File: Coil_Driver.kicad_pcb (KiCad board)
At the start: 8 copper layers, 122.5 x 76 mm, 158 parts, among them J1 47346-0001, J3 NPPC122KFMS-RC, U1 SG-210STF 12.0000ML3, U10 ADP7142ARDZ-R7, U11 BUK9D23-40E, U12 BUK9D23-40E, U13 ADuM4120-1A, U14 ADuM4120-1A, U15 LT8253AJUFDM#PBF, U16 PSMNR55-40SSH, U17 PSMNR55-40SSH, U18 PSMNR55-40SSH, U19 PSMNR55-40SSH, U2 ICE40UP5K-SG48ITR, U20 BUK9D23-40E, U21 BUK9D23-40E, U22 PSMNR55-40SSH, U23 PSMNR55-40SSH, U24 PSMNR55-40SSH, U25 PSMNR55-40SSH, U26 LT3748, U27 BUK9D23-40E, U28 ADuM4120-1A, U29 ADuM4120-1A, U3 W25Q32JVSS, U4 SN74AUP2G125DCUR, U5 AP2127K-3.3, U6 LT1117CST#TRPBF, U7 AP2127K-1.2, U8 93LC56BT-I/OT, U9 FT232H

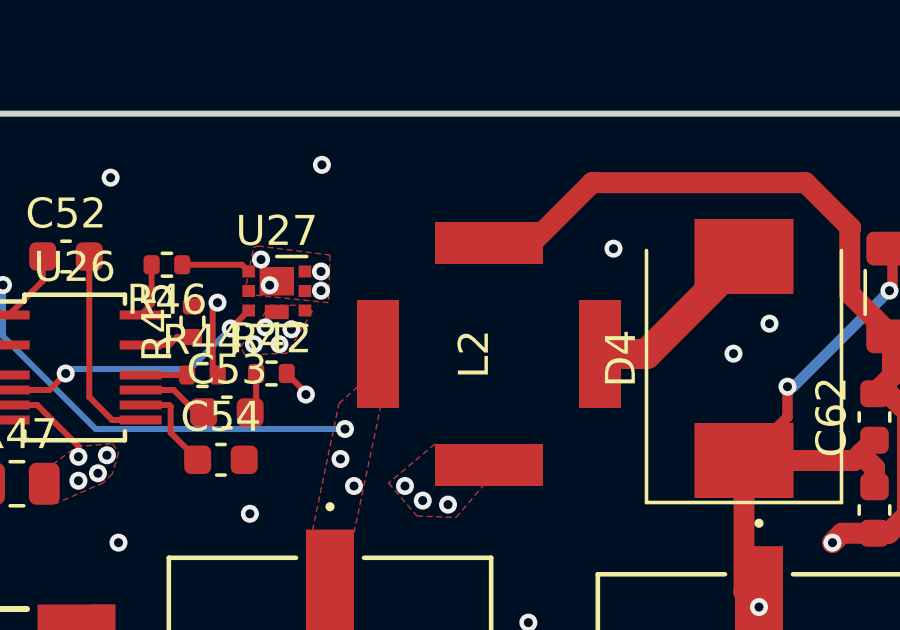
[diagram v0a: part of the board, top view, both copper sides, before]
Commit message: Rotated L2 90° clockwise
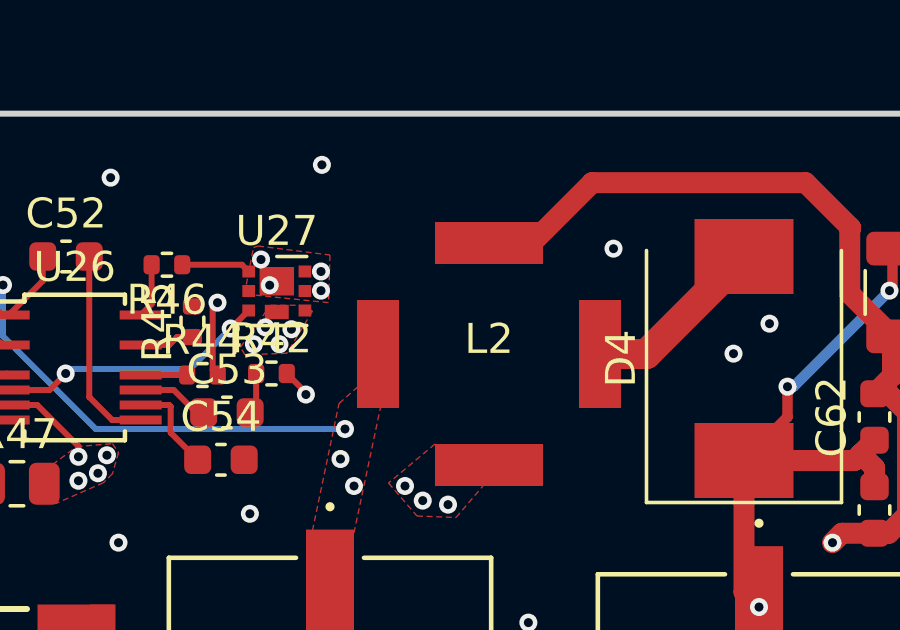
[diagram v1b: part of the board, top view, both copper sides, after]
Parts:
- turned L2 to 0 degrees
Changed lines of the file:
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@@
 	(footprint "New_Library:WE-TDC-8018"
 		(layer "F.Cu")
-		(at 85.45 32.01125 90)
+		(at 85.45 32.01125)
 		(property "Reference" "L2"
-			(at 0 -0.5 90)
+			(at 0 -0.5 0)
 			(unlocked yes)
 			(layer "F.SilkS")
@@
 		)
 		(property "Value" "74489430010"
-			(at 0 1 90)
+			(at 0 1 0)
 			(unlocked yes)
 			(layer "F.Fab")
@@
 		)
 		(property "Footprint" "New_Library:WE-TDC-8018"
-			(at 0 0 90)
+			(at 0 0 0)
 			(unlocked yes)
 			(layer "F.Fab")
@@
 		)
 		(property "Datasheet" "https://www.we-online.com/components/products/datasheet/74489430010.pdf"
-			(at 0 0 90)
+			(at 0 0 0)
 			(unlocked yes)
 			(layer "F.Fab")
@@
 		)
 		(property "Description" "1µ, 2.85a"
-			(at 0 0 90)
+			(at 0 0 0)
 			(unlocked yes)
 			(layer "F.Fab")
@@
 		)
 		(property "Sim.Device" "L"
-			(at 0 0 90)
+			(at 0 0 0)
 			(unlocked yes)
 			(layer "F.Fab")
@@
 		)
 		(property "Sim.Params" "L=74489430010"
-			(at 0 0 90)
+			(at 0 0 0)
 			(unlocked yes)
 			(layer "F.Fab")
@@
 		)
 		(fp_line
+			(start -4.6 -2)
+			(end -2 -4.6)
+			(stroke
+				(width 0.1)
+				(type default)
+			)
+			(layer "F.CrtYd")
+		)
+		(fp_line
+			(start -4.6 2)
+			(end -4.6 -2)
+			(stroke
+				(width 0.1)
+				(type default)
+			)
+			(layer "F.CrtYd")
+		)
+		(fp_line
+			(start -2 -4.6)
+			(end 2 -4.6)
+			(stroke
+				(width 0.1)
+				(type default)
+			)
+			(layer "F.CrtYd")
+		)
+		(fp_line
+			(start -2 4.6)
+			(end -4.6 2)
+			(stroke
+				(width 0.1)
+				(type default)
+			)
+			(layer "F.CrtYd")
+		)
+		(fp_line
 			(start 2 -4.6)
 			(end 4.6 -2)
@@
 		)
 		(fp_line
-			(start -2 -4.6)
-			(end 2 -4.6)
+			(start 2 4.6)
+			(end -2 4.6)
 			(stroke
 				(width 0.1)
@@
 		)
 		(fp_line
-			(start -4.6 -2)
-			(end -2 -4.6)
-			(stroke
-				(width 0.1)
-				(type default)
-			)
-			(layer "F.CrtYd")
-		)
-		(fp_line
 			(start 4.6 2)
 			(end 2 4.6)
@@
 			(layer "F.CrtYd")
 		)
-		(fp_line
-			(start -4.6 2)
-			(end -4.6 -2)
-			(stroke
-				(width 0.1)
-				(type default)
-			)
-			(layer "F.CrtYd")
-		)
-		(fp_line
-			(start 2 4.6)
-			(end -2 4.6)
-			(stroke
-				(width 0.1)
-				(type default)
-			)
-			(layer "F.CrtYd")
-		)
-		(fp_line
-			(start -2 4.6)
-			(end -4.6 2)
-			(stroke
-				(width 0.1)
-				(type default)
-			)
-			(layer "F.CrtYd")
-		)
 		(fp_text user "${REFERENCE}"
-			(at 0 2.5 90)
+			(at 0 2.5 0)
 			(unlocked yes)
 			(layer "F.Fab")
@@
 		)
 		(pad "1" smd rect
-			(at 0 -3.7 270)
+			(at 0 -3.7 180)
 			(size 3.6 1.4)
 			(layers "F.Cu" "F.Paste" "F.Mask")
@@
 		)
 		(pad "2" smd rect
-			(at -3.7 0 180)
+			(at -3.7 0 90)
 			(size 3.6 1.4)
 			(layers "F.Cu" "F.Paste" "F.Mask")
@@
 		)
 		(pad "3" smd rect
-			(at 0 3.7 270)
+			(at 0 3.7 180)
 			(size 3.6 1.4)
 			(layers "F.Cu" "F.Paste" "F.Mask")
@@
 		)
 		(pad "4" smd rect
-			(at 3.7 0)
+			(at 3.7 0 270)
 			(size 3.6 1.4)
 			(layers "F.Cu" "F.Paste" "F.Mask")
@@
 			(polygon
 				(pts
-					(xy 82.35 30.21125) (xy 83.65 28.91125) (xy 87.25 28.91125) (xy 88.55 30.21125) (xy 88.55 33.81125)
-					(xy 87.25 35.11125) (xy 83.65 35.11125) (xy 82.35 33.81125)
-				)
-			)
+					(xy 87.25 28.91125) (xy 88.55 30.21125) (xy 88.55 33.81125) (xy 87.25 35.11125) (xy 83.65 35.11125)
+					(xy 82.35 33.81125) (xy 82.35 30.21125) (xy 83.65 28.91125)
+				)
+			)

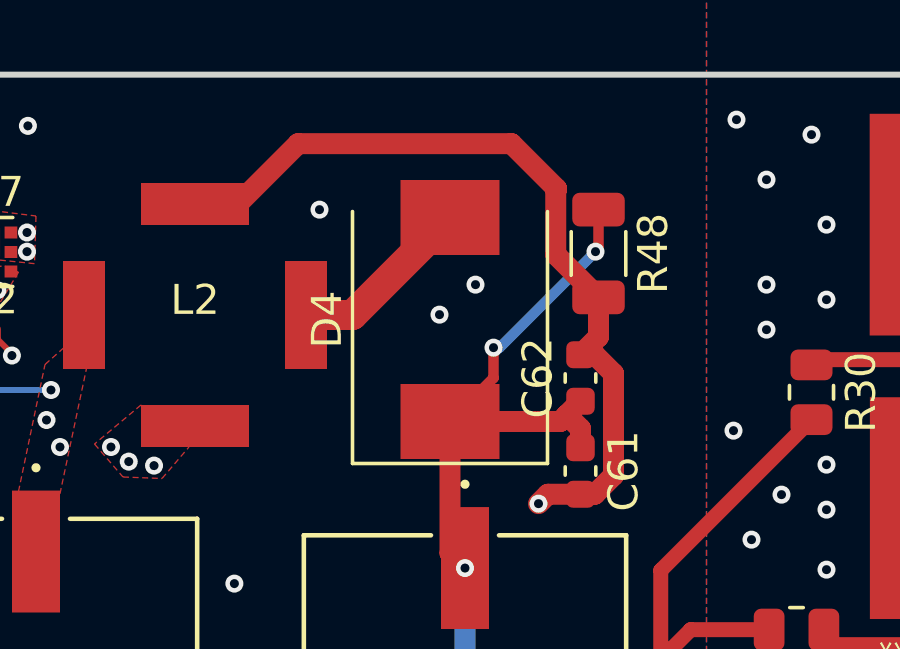
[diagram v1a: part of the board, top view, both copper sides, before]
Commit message: Fixed L2 symbol and PCB orientation
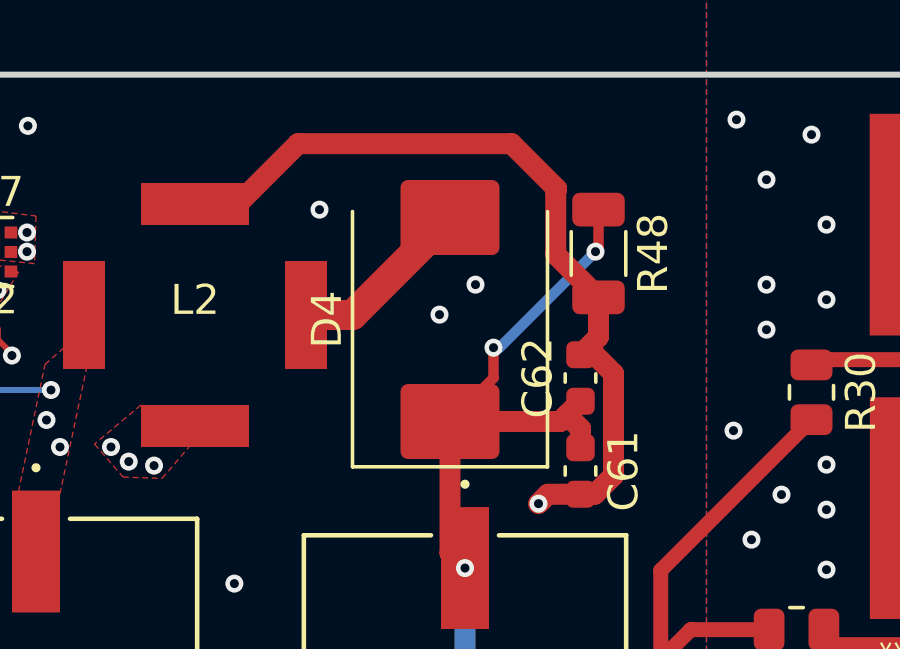
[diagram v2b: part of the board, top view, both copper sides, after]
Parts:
- R28, R47: value ESR10EZPF5R10 -> CRF0805-FZ-R005ELF
- R35: value 98.8k -> 95.3k
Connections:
- L2 pad 1: 10.5V -> GND2
- L2 pad 2: /toInductor -> 10.5V
- L2 pad 3: Net-(D4-A) -> /toInductor
- L2 pad 4: GND2 -> Net-(D4-A)
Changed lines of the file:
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@@
 			(size 3.6 1.4)
 			(layers "F.Cu" "F.Paste" "F.Mask")
-			(net 7 "10.5V")
-			(pinfunction "A")
+			(net 23 "GND2")
+			(pinfunction "1")
 			(pintype "passive")
 			(thermal_bridge_angle 45)
@@
 			(size 3.6 1.4)
 			(layers "F.Cu" "F.Paste" "F.Mask")
-			(net 134 "/toInductor")
-			(pinfunction "B")
+			(net 7 "10.5V")
+			(pinfunction "2")
 			(pintype "passive")
 			(thermal_bridge_angle 45)
@@
 			(size 3.6 1.4)
 			(layers "F.Cu" "F.Paste" "F.Mask")
-			(net 38 "Net-(D4-A)")
-			(pinfunction "B")
+			(net 134 "/toInductor")
+			(pinfunction "3")
 			(pintype "passive")
 			(thermal_bridge_angle 45)
@@
 			(size 3.6 1.4)
 			(layers "F.Cu" "F.Paste" "F.Mask")
-			(net 23 "GND2")
-			(pinfunction "A")
+			(net 38 "Net-(D4-A)")
+			(pinfunction "4")
 			(pintype "passive")
 			(thermal_bridge_angle 45)
@@
 			)
 		)
-		(model "/home/yeuph/Downloads/74489430010 (1)/Download_STP_WE-TDC-8018_rev1.stp"
-			(offset
-				(xyz 0 0 0)
-			)
-			(scale
-				(xyz 1 1 1)
-			)
-			(rotate
-				(xyz 0 0 0)
-			)
-		)
 	)
 	(footprint "Oscillator:Oscillator_SMD_SeikoEpson_SG210-4Pin_2.5x2.0mm"
@@
 			)
 		)
-		(property "Value" "98.8k"
+		(property "Value" "95.3k"
 			(at 0 1.17 0)
 			(layer "F.Fab")
@@
 			)
 		)
-		(property "Sim.Params" "R=98.8k"
+		(property "Sim.Params" "R=95.3k"
 			(at 0 0 180)
 			(unlocked yes)
@@
 		(attr smd)
 		(fp_line
-			(start -4.8 -3.25)
+			(start -4.91 -3.25)
 			(end 3.6 -3.25)
 			(stroke
@@
 		)
 		(fp_line
-			(start -4.8 3.25)
-			(end -4.8 -3.25)
+			(start -4.91 3.25)
+			(end -4.91 -3.25)
 			(stroke
 				(width 0.12)
@@
 		)
 		(fp_line
-			(start -4.8 3.25)
+			(start -4.91 3.25)
 			(end 3.6 3.25)
 			(stroke
@@
 			)
 		)
-		(pad "1" smd rect
+		(pad "1" smd roundrect
 			(at -3.4 0 180)
 			(size 3.3 2.5)
 			(layers "F.Cu" "F.Paste" "F.Mask")
+			(roundrect_rratio 0.1)
 			(net 22 "ISO_10.5")
 			(pinfunction "K")
 			(pintype "passive")
 		)
-		(pad "2" smd rect
+		(pad "2" smd roundrect
 			(at 3.4 0 180)
 			(size 3.3 2.5)
 			(layers "F.Cu" "F.Paste" "F.Mask")
+			(roundrect_rratio 0.1)
 			(net 38 "Net-(D4-A)")
 			(pinfunction "A")
 			(pintype "passive")
 		)
-		(model "${KICAD6_3DMODEL_DIR}/Diode_SMD.3dshapes/D_SMC.wrl"
+		(model "${KICAD8_3DMODEL_DIR}/Diode_SMD.3dshapes/D_SMC.wrl"
 			(offset
 				(xyz 0 0 0)
@@
 			)
 		)
-		(property "Value" "ESR10EZPF5R10"
+		(property "Value" "CRF0805-FZ-R005ELF"
 			(at 0 1.65 0)
 			(layer "F.Fab")
@@
 			)
 		)
-		(property "Datasheet" "https://fscdn.rohm.com/en/products/databook/datasheet/passive/resistor/chip_resistor/esr-e.pdf"
+		(property "Datasheet" "https://bourns.com/docs/Product-Datasheets/CRF.pdf"
 			(at 0 0 0)
 			(layer "F.Fab")
@@
 			)
 		)
-		(property "Description" "RES 5.1 OHM 1% 1/2W 0805"
+		(property "Description" "RES 5m 1% 1/2W 0805"
 			(at 0 0 0)
 			(layer "F.Fab")
@@
 			)
 		)
-		(property "Sim.Params" "R=ESR10EZPF5R10"
+		(property "Sim.Params" "R=CRF0805-FZ-R005ELF"
 			(at 0 0 0)
 			(unlocked yes)
@@
 			)
 		)
-		(property "Value" "ESR10EZPF5R10"
+		(property "Value" "CRF0805-FZ-R005ELF"
 			(at -0.2125 -3.5 0)
 			(layer "F.Fab")
@@
 			)
 		)
-		(property "Datasheet" "https://fscdn.rohm.com/en/products/databook/datasheet/passive/resistor/chip_resistor/esr-e.pdf"
+		(property "Datasheet" "https://bourns.com/docs/Product-Datasheets/CRF.pdf"
 			(at 0 0 0)
 			(layer "F.Fab")
@@
 			)
 		)
-		(property "Description" "RES 5.1 OHM 1% 1/2W 0805"
+		(property "Description" "RES 5 mOHM 1% 1/2W 0805"
 			(at 0 0 0)
 			(layer "F.Fab")
@@
 			)
 		)
-		(property "Sim.Params" "R=ESR10EZPF5R10"
+		(property "Sim.Params" "R=CRF0805-FZ-R005ELF"
 			(at 0 0 0)
 			(unlocked yes)
